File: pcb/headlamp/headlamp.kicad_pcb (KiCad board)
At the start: 2 copper layers, 34 x 34 mm, 60 parts, among them IC1 ATTINY841-SSU, P1 POWER, P2 SERIAL, P3 ISP, Q1 VEMT3700-GS08, Q2 NX2301P, Q3 DMP2035U, Q4 DMP2035U, SW1 BT2, SW2 BT1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

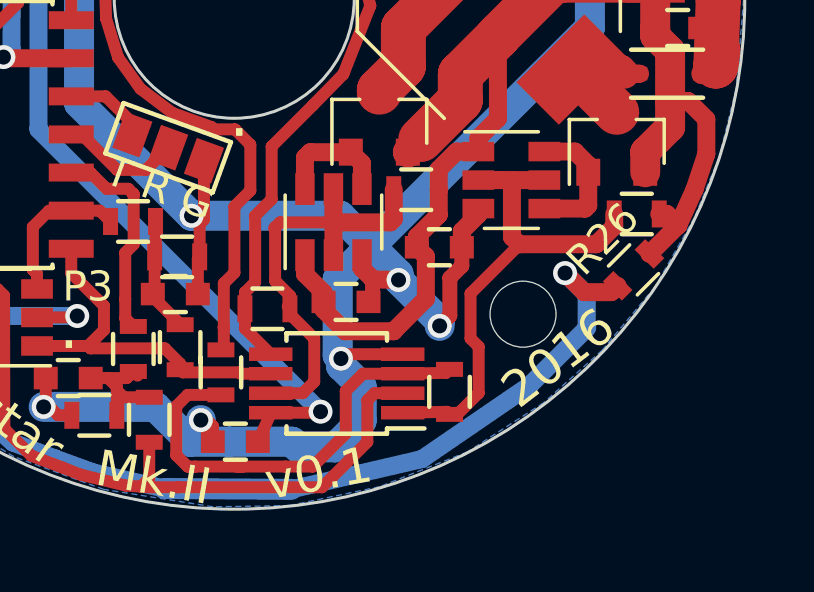
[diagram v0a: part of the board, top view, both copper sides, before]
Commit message: Remove voltage spikes building up
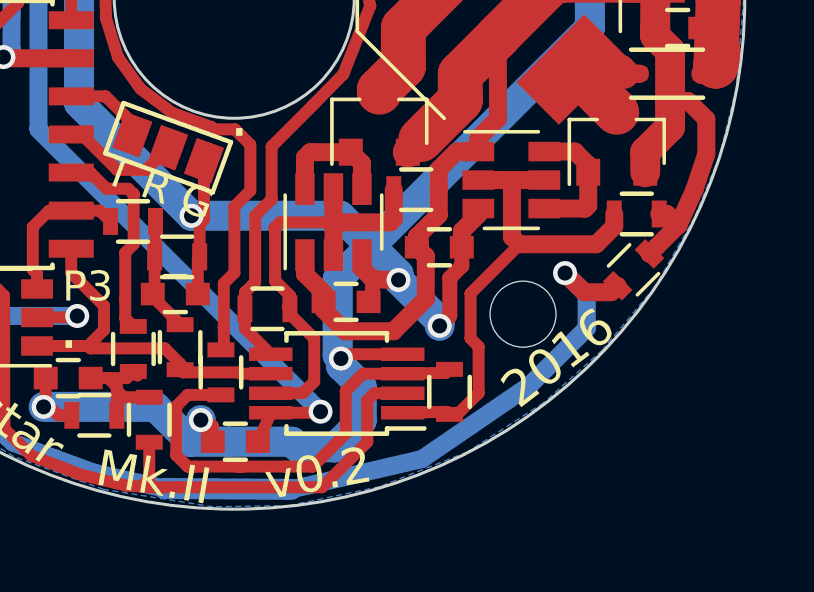
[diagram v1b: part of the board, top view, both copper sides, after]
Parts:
- R5: value 10k -> 100k
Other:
- board text added: "v0.2"
- board text removed: "v0.1"
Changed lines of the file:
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@@
     (title "Darkstar Mk.II")
     (date 2016-12-28)
-    (rev 0.1)
+    (rev 0.2)
     (company "Jakub Kaderka")
   )
@@
   )
   (setup
-    (last_trace_width 0.6)
+    (last_trace_width 0.25)
     (user_trace_width 0.4)
     (user_trace_width 0.5)
@@
       (effects (font (size 1 1) (thickness 0.15)))
     )
-    (fp_text value 10k (at 0 1.9) (layer F.Fab)
+    (fp_text value 100k (at 0 1.9) (layer F.Fab)
       (effects (font (size 1 1) (thickness 0.15)))
     )
@@
     (tags "resistor 0603")
     (attr smd)
-    (fp_text reference R26 (at 0 -1.45 45) (layer F.SilkS)
+    (fp_text reference R26 (at 0 -1.45 45) (layer F.SilkS) hide
       (effects (font (size 1 1) (thickness 0.15)))
     )
@@
       (effects (font (size 1 1) (thickness 0.15)))
     )
-    (fp_text user %R (at 0 -1.45 45) (layer F.Fab)
+    (fp_text user %R (at 0 -1.45 45) (layer F.Fab) hide
       (effects (font (size 1 1) (thickness 0.15)))
     )
@@
     (effects (font (size 1.5 1.5) (thickness 0.3)))
   )
-  (gr_text v0.1 (at 143.98 125.34 10) (layer F.SilkS)
+  (gr_text v0.2 (at 143.98 125.34 10) (layer F.SilkS)
     (effects (font (size 1.2 1.2) (thickness 0.25)))
   )
